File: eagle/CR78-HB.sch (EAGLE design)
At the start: 35 parts, among them Q1 2N3904, Q2 2N3904, Q3 2N3904

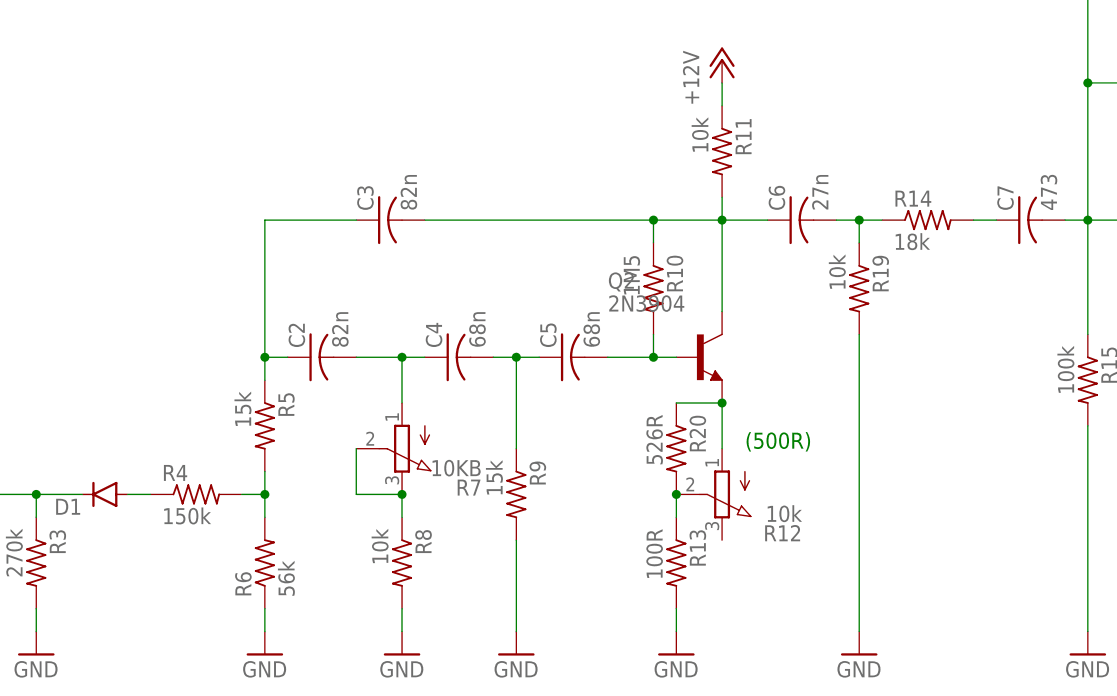
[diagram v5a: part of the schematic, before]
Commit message: values for LC
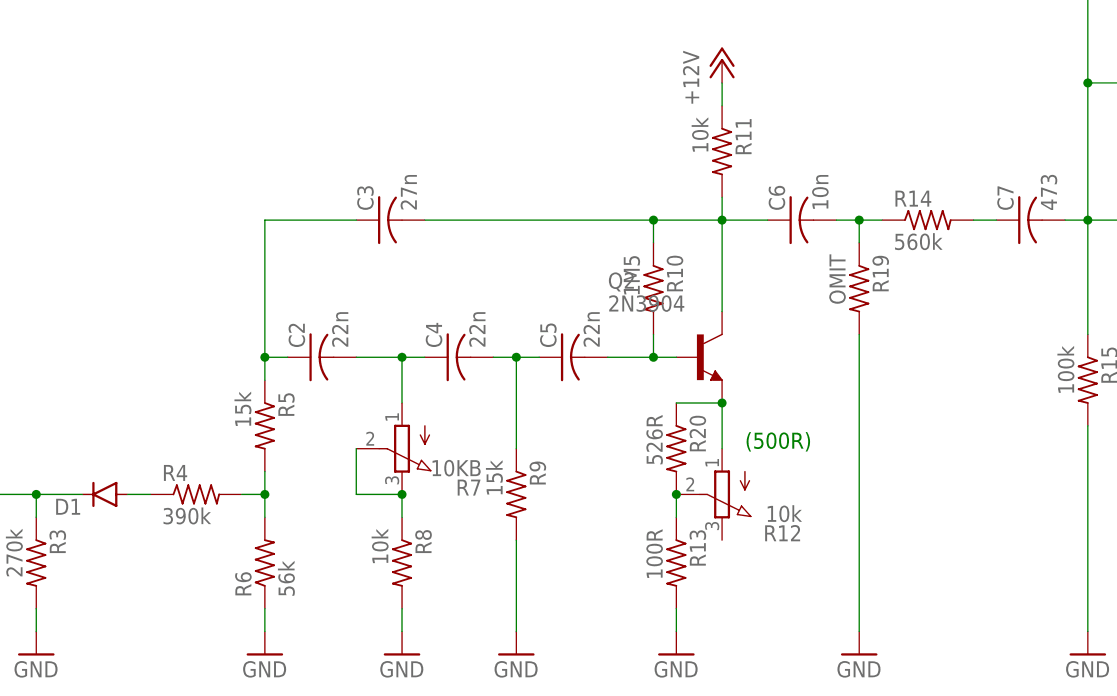
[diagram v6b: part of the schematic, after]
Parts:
- C2: value 82n -> 22n
- C3: value 82n -> 27n
- C4, C5: value 68n -> 22n
- C6: value 27n -> 10n
- R14: value 18k -> 560k
- R19: value 10k -> OMIT
- R4: value 150k -> 390k
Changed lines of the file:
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@@
 <?xml version="1.0" encoding="utf-8"?>
 <!DOCTYPE eagle SYSTEM "eagle.dtd">
-<eagle version="7.6.0">
+<eagle version="7.1.0">
 <drawing>
 <settings>
@@
 <grid distance="0.1" unitdist="inch" unit="inch" style="lines" multiple="1" display="no" altdistance="0.01" altunitdist="inch" altunit="inch"/>
 <layers>
-<layer number="1" name="Top" color="4" fill="1" visible="yes" active="no"/>
-<layer number="16" name="Bottom" color="1" fill="1" visible="yes" active="no"/>
-<layer number="17" name="Pads" color="2" fill="1" visible="yes" active="no"/>
-<layer number="18" name="Vias" color="2" fill="1" visible="yes" active="no"/>
-<layer number="19" name="Unrouted" color="6" fill="1" visible="yes" active="no"/>
-<layer number="20" name="Dimension" color="15" fill="1" visible="yes" active="no"/>
-<layer number="21" name="tPlace" color="7" fill="1" visible="yes" active="no"/>
-<layer number="22" name="bPlace" color="7" fill="1" visible="yes" active="no"/>
-<layer number="23" name="tOrigins" color="15" fill="1" visible="yes" active="no"/>
-<layer number="24" name="bOrigins" color="15" fill="1" visible="yes" active="no"/>
-<layer number="25" name="tNames" color="7" fill="1" visible="yes" active="no"/>
-<layer number="26" name="bNames" color="7" fill="1" visible="yes" active="no"/>
-<layer number="27" name="tValues" color="7" fill="1" visible="yes" active="no"/>
-<layer number="28" name="bValues" color="7" fill="1" visible="yes" active="no"/>
+<layer number="1" name="Top" color="4" fill="1" visible="no" active="no"/>
+<layer number="16" name="Bottom" color="1" fill="1" visible="no" active="no"/>
+<layer number="17" name="Pads" color="2" fill="1" visible="no" active="no"/>
+<layer number="18" name="Vias" color="2" fill="1" visible="no" active="no"/>
+<layer number="19" name="Unrouted" color="6" fill="1" visible="no" active="no"/>
+<layer number="20" name="Dimension" color="15" fill="1" visible="no" active="no"/>
+<layer number="21" name="tPlace" color="7" fill="1" visible="no" active="no"/>
+<layer number="22" name="bPlace" color="7" fill="1" visible="no" active="no"/>
+<layer number="23" name="tOrigins" color="15" fill="1" visible="no" active="no"/>
+<layer number="24" name="bOrigins" color="15" fill="1" visible="no" active="no"/>
+<layer number="25" name="tNames" color="7" fill="1" visible="no" active="no"/>
+<layer number="26" name="bNames" color="7" fill="1" visible="no" active="no"/>
+<layer number="27" name="tValues" color="7" fill="1" visible="no" active="no"/>
+<layer number="28" name="bValues" color="7" fill="1" visible="no" active="no"/>
 <layer number="29" name="tStop" color="7" fill="3" visible="no" active="no"/>
 <layer number="30" name="bStop" color="7" fill="6" visible="no" active="no"/>
@@
 <layer number="35" name="tGlue" color="7" fill="4" visible="no" active="no"/>
 <layer number="36" name="bGlue" color="7" fill="5" visible="no" active="no"/>
-<layer number="37" name="tTest" color="7" fill="1" visible="yes" active="no"/>
-<layer number="38" name="bTest" color="7" fill="1" visible="yes" active="no"/>
+<layer number="37" name="tTest" color="7" fill="1" visible="no" active="no"/>
+<layer number="38" name="bTest" color="7" fill="1" visible="no" active="no"/>
 <layer number="39" name="tKeepout" color="4" fill="11" visible="no" active="no"/>
 <layer number="40" name="bKeepout" color="1" fill="11" visible="no" active="no"/>
@@
 <layer number="44" name="Drills" color="7" fill="1" visible="no" active="no"/>
 <layer number="45" name="Holes" color="7" fill="1" visible="no" active="no"/>
-<layer number="46" name="Milling" color="3" fill="1" visible="yes" active="no"/>
-<layer number="47" name="Measures" color="7" fill="1" visible="yes" active="no"/>
-<layer number="48" name="Document" color="7" fill="1" visible="yes" active="no"/>
-<layer number="49" name="Reference" color="7" fill="1" visible="yes" active="no"/>
-<layer number="50" name="dxf" color="7" fill="1" visible="yes" active="no"/>
-<layer number="51" name="tDocu" color="7" fill="1" visible="yes" active="no"/>
-<layer number="52" name="bDocu" color="7" fill="1" visible="yes" active="no"/>
-<layer number="53" name="tGND_GNDA" color="7" fill="9" visible="yes" active="no"/>
-<layer number="54" name="bGND_GNDA" color="1" fill="9" visible="yes" active="no"/>
-<layer number="56" name="wert" color="7" fill="1" visible="yes" active="no"/>
-<layer number="57" name="tCAD" color="7" fill="1" visible="yes" active="no"/>
-<layer number="59" name="tCarbon" color="7" fill="1" visible="yes" active="no"/>
-<layer number="60" name="bCarbon" color="7" fill="1" visible="yes" active="no"/>
+<layer number="46" name="Milling" color="3" fill="1" visible="no" active="no"/>
+<layer number="47" name="Measures" color="7" fill="1" visible="no" active="no"/>
+<layer number="48" name="Document" color="7" fill="1" visible="no" active="no"/>
+<layer number="49" name="Reference" color="7" fill="1" visible="no" active="no"/>
+<layer number="50" name="dxf" color="7" fill="1" visible="no" active="no"/>
+<layer number="51" name="tDocu" color="7" fill="1" visible="no" active="no"/>
+<layer number="52" name="bDocu" color="7" fill="1" visible="no" active="no"/>
+<layer number="53" name="tGND_GNDA" color="7" fill="9" visible="no" active="no"/>
+<layer number="54" name="bGND_GNDA" color="1" fill="9" visible="no" active="no"/>
+<layer number="56" name="wert" color="7" fill="1" visible="no" active="no"/>
+<layer number="57" name="tCAD" color="7" fill="1" visible="no" active="no"/>
+<layer number="59" name="tCarbon" color="7" fill="1" visible="no" active="no"/>
+<layer number="60" name="bCarbon" color="7" fill="1" visible="no" active="no"/>
 <layer number="90" name="Modules" color="5" fill="1" visible="yes" active="yes"/>
 <layer number="91" name="Nets" color="2" fill="1" visible="yes" active="yes"/>
@@
 <part name="D1" library="SparkFun-DiscreteSemi" deviceset="DIODE" device="1N4148"/>
 <part name="GND3" library="supply1" deviceset="GND" device=""/>
-<part name="R4" library="rcl" deviceset="R-US_" device="0207/7" value="150k"/>
+<part name="R4" library="rcl" deviceset="R-US_" device="0207/7" value="390k"/>
 <part name="R6" library="rcl" deviceset="R-US_" device="0207/7" value="56k"/>
 <part name="R5" library="rcl" deviceset="R-US_" device="0207/7" value="15k"/>
-<part name="C2" library="rcl" deviceset="C-US" device="050-025X075" value="82n"/>
-<part name="C3" library="rcl" deviceset="C-US" device="050-025X075" value="82n"/>
-<part name="C4" library="rcl" deviceset="C-US" device="050-025X075" value="68n"/>
+<part name="C2" library="rcl" deviceset="C-US" device="050-025X075" value="22n"/>
+<part name="C3" library="rcl" deviceset="C-US" device="050-025X075" value="27n"/>
+<part name="C4" library="rcl" deviceset="C-US" device="050-025X075" value="22n"/>
 <part name="R8" library="rcl" deviceset="R-US_" device="0207/7" value="10k"/>
 <part name="R7" library="pot" deviceset="3RP/1610N" device="" value="10KB"/>
-<part name="C5" library="rcl" deviceset="C-US" device="050-025X075" value="68n"/>
+<part name="C5" library="rcl" deviceset="C-US" device="050-025X075" value="22n"/>
 <part name="R9" library="rcl" deviceset="R-US_" device="0207/5V" value="15k"/>
 <part name="Q2" library="808_lt" deviceset="2N3904" device=""/>
@@
 <part name="R10" library="rcl" deviceset="R-US_" device="0207/7" value="1M5"/>
 <part name="R11" library="rcl" deviceset="R-US_" device="0207/7" value="10k"/>
-<part name="R14" library="rcl" deviceset="R-US_" device="0207/7" value="18k"/>
-<part name="C6" library="rcl" deviceset="C-US" device="050-025X075" value="27n"/>
+<part name="R14" library="rcl" deviceset="R-US_" device="0207/7" value="560k"/>
+<part name="C6" library="rcl" deviceset="C-US" device="050-025X075" value="10n"/>
 <part name="R12" library="pot" deviceset="3RP/1610N" device="" value="10k"/>
 <part name="GND4" library="supply1" deviceset="GND" device=""/>
@@
 <part name="R15" library="rcl" deviceset="R-US_" device="0207/7" value="100k"/>
 <part name="GND8" library="supply1" deviceset="GND" device=""/>
-<part name="R19" library="rcl" deviceset="R-US_" device="0207/5V" value="10k"/>
+<part name="R19" library="rcl" deviceset="R-US_" device="0207/5V" value="OMIT"/>
 <part name="GND12" library="supply1" deviceset="GND" device=""/>
 <part name="BD" library="con-molex" deviceset="22-23-2041" device=""/>

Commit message: values for LB
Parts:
- C2, C4: value 22n -> 12n
- C3: value 27n -> 18n
- C5: value 22n -> 10n
- C6: value 10n -> 8n2
- R14: value 560k -> 680k
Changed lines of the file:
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@@
 <part name="R6" library="rcl" deviceset="R-US_" device="0207/7" value="56k"/>
 <part name="R5" library="rcl" deviceset="R-US_" device="0207/7" value="15k"/>
-<part name="C2" library="rcl" deviceset="C-US" device="050-025X075" value="22n"/>
-<part name="C3" library="rcl" deviceset="C-US" device="050-025X075" value="27n"/>
-<part name="C4" library="rcl" deviceset="C-US" device="050-025X075" value="22n"/>
+<part name="C2" library="rcl" deviceset="C-US" device="050-025X075" value="12n"/>
+<part name="C3" library="rcl" deviceset="C-US" device="050-025X075" value="18n"/>
+<part name="C4" library="rcl" deviceset="C-US" device="050-025X075" value="12n"/>
 <part name="R8" library="rcl" deviceset="R-US_" device="0207/7" value="10k"/>
 <part name="R7" library="pot" deviceset="3RP/1610N" device="" value="10KB"/>
-<part name="C5" library="rcl" deviceset="C-US" device="050-025X075" value="22n"/>
+<part name="C5" library="rcl" deviceset="C-US" device="050-025X075" value="10n"/>
 <part name="R9" library="rcl" deviceset="R-US_" device="0207/5V" value="15k"/>
 <part name="Q2" library="808_lt" deviceset="2N3904" device=""/>
@@
 <part name="R10" library="rcl" deviceset="R-US_" device="0207/7" value="1M5"/>
 <part name="R11" library="rcl" deviceset="R-US_" device="0207/7" value="10k"/>
-<part name="R14" library="rcl" deviceset="R-US_" device="0207/7" value="560k"/>
-<part name="C6" library="rcl" deviceset="C-US" device="050-025X075" value="10n"/>
+<part name="R14" library="rcl" deviceset="R-US_" device="0207/7" value="680k"/>
+<part name="C6" library="rcl" deviceset="C-US" device="050-025X075" value="8n2"/>
 <part name="R12" library="pot" deviceset="3RP/1610N" device="" value="10k"/>
 <part name="GND4" library="supply1" deviceset="GND" device=""/>

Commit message: values for HB
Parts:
- C2: value 12n -> 8n2
- C3: value 18n -> 8n2
- C4: value 12n -> 6n8
- C5: value 10n -> 6n8
- C6: value 8n2 -> 2n2
- R14: value 680k -> 1M5
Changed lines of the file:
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@@
 <part name="R6" library="rcl" deviceset="R-US_" device="0207/7" value="56k"/>
 <part name="R5" library="rcl" deviceset="R-US_" device="0207/7" value="15k"/>
-<part name="C2" library="rcl" deviceset="C-US" device="050-025X075" value="12n"/>
-<part name="C3" library="rcl" deviceset="C-US" device="050-025X075" value="18n"/>
-<part name="C4" library="rcl" deviceset="C-US" device="050-025X075" value="12n"/>
+<part name="C2" library="rcl" deviceset="C-US" device="050-025X075" value="8n2"/>
+<part name="C3" library="rcl" deviceset="C-US" device="050-025X075" value="8n2"/>
+<part name="C4" library="rcl" deviceset="C-US" device="050-025X075" value="6n8"/>
 <part name="R8" library="rcl" deviceset="R-US_" device="0207/7" value="10k"/>
 <part name="R7" library="pot" deviceset="3RP/1610N" device="" value="10KB"/>
-<part name="C5" library="rcl" deviceset="C-US" device="050-025X075" value="10n"/>
+<part name="C5" library="rcl" deviceset="C-US" device="050-025X075" value="6n8"/>
 <part name="R9" library="rcl" deviceset="R-US_" device="0207/5V" value="15k"/>
 <part name="Q2" library="808_lt" deviceset="2N3904" device=""/>
@@
 <part name="R10" library="rcl" deviceset="R-US_" device="0207/7" value="1M5"/>
 <part name="R11" library="rcl" deviceset="R-US_" device="0207/7" value="10k"/>
-<part name="R14" library="rcl" deviceset="R-US_" device="0207/7" value="680k"/>
-<part name="C6" library="rcl" deviceset="C-US" device="050-025X075" value="8n2"/>
+<part name="R14" library="rcl" deviceset="R-US_" device="0207/7" value="1M5"/>
+<part name="C6" library="rcl" deviceset="C-US" device="050-025X075" value="2n2"/>
 <part name="R12" library="pot" deviceset="3RP/1610N" device="" value="10k"/>
 <part name="GND4" library="supply1" deviceset="GND" device=""/>
